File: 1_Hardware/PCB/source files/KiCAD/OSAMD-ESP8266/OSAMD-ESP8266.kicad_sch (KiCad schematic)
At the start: 20 parts, among them J1 DHT-Socket, J2 MQ-135 Conn, J3 LCD Conn, J6 USB_B, J7 Socket_D1_Mini_01_08, J8 Socket_D1_Mini_09_16, SW1 SW_Pushbutton, U1 WeMos_D1_mini

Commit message: switched button and buzzer pin
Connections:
- net BTN: now also J8.3 (Pin_3), U1.11 (D4); no longer J7.7 (Pin_7), U1.7 (CS/D8)
- net BUZZER: now also J7.7 (Pin_7), U1.7 (CS/D8); no longer J8.3 (Pin_3), U1.11 (D4)
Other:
- moved on the sheet: PullupBTN1, SW1

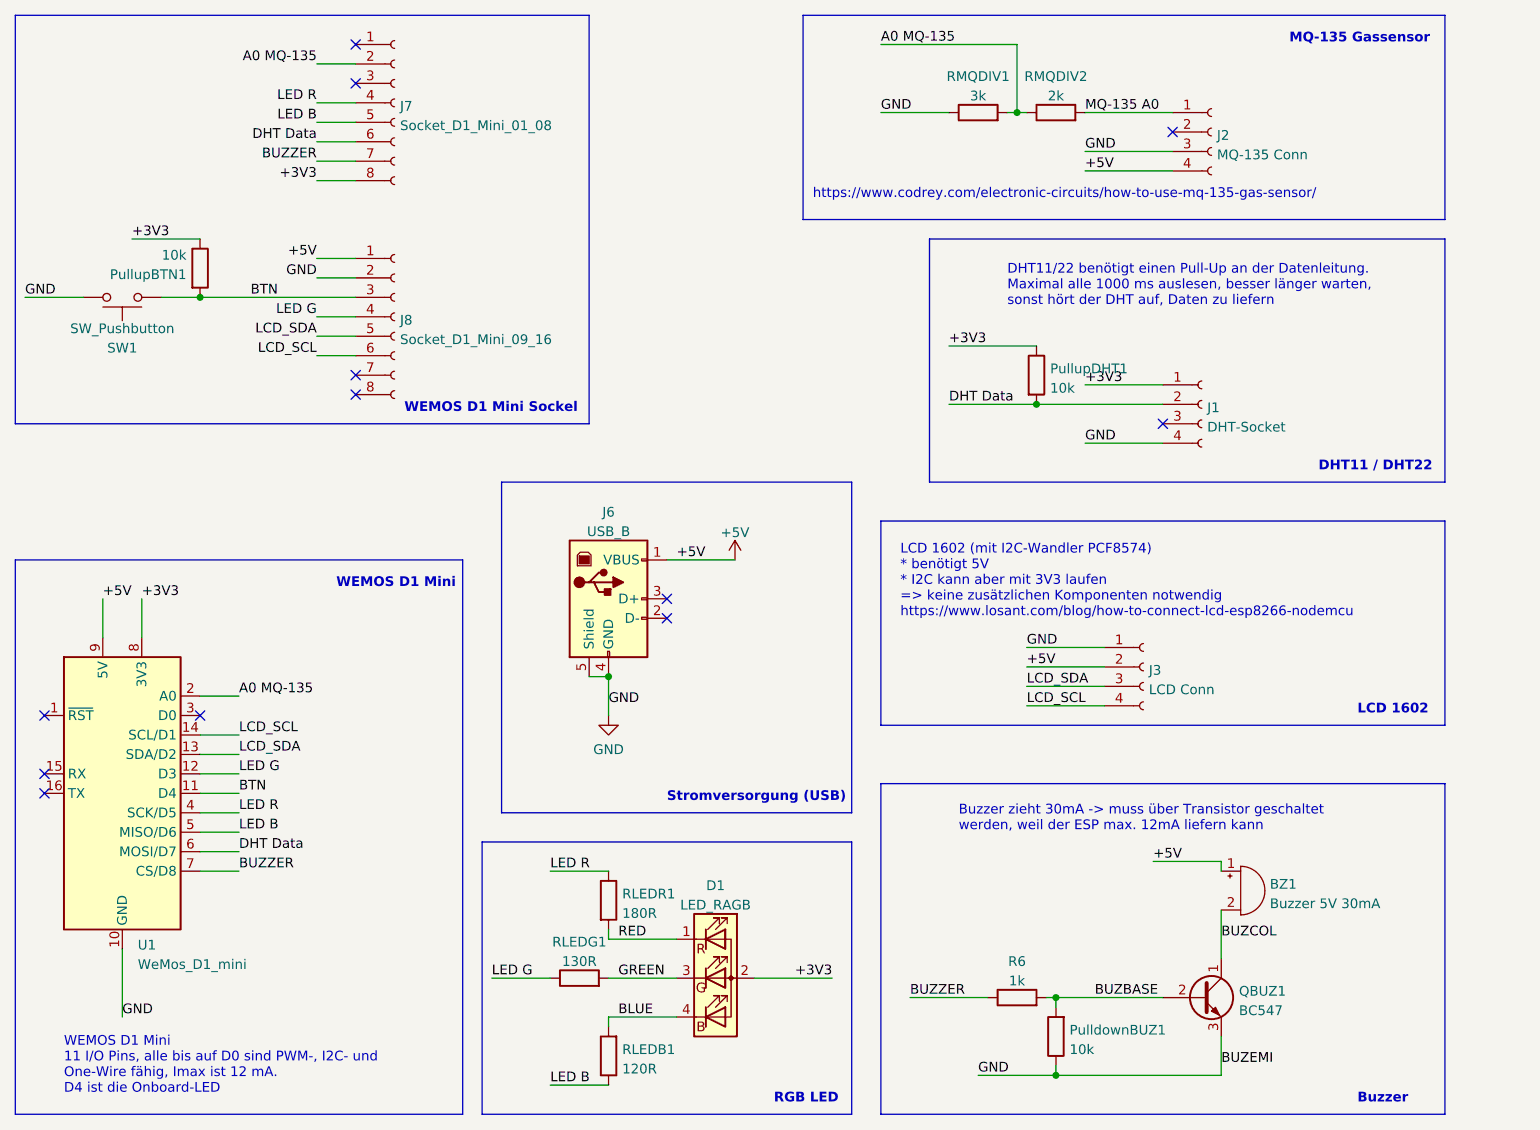
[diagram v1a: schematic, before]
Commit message: rounded edges on the pcb set gerber settings for jlcpcb
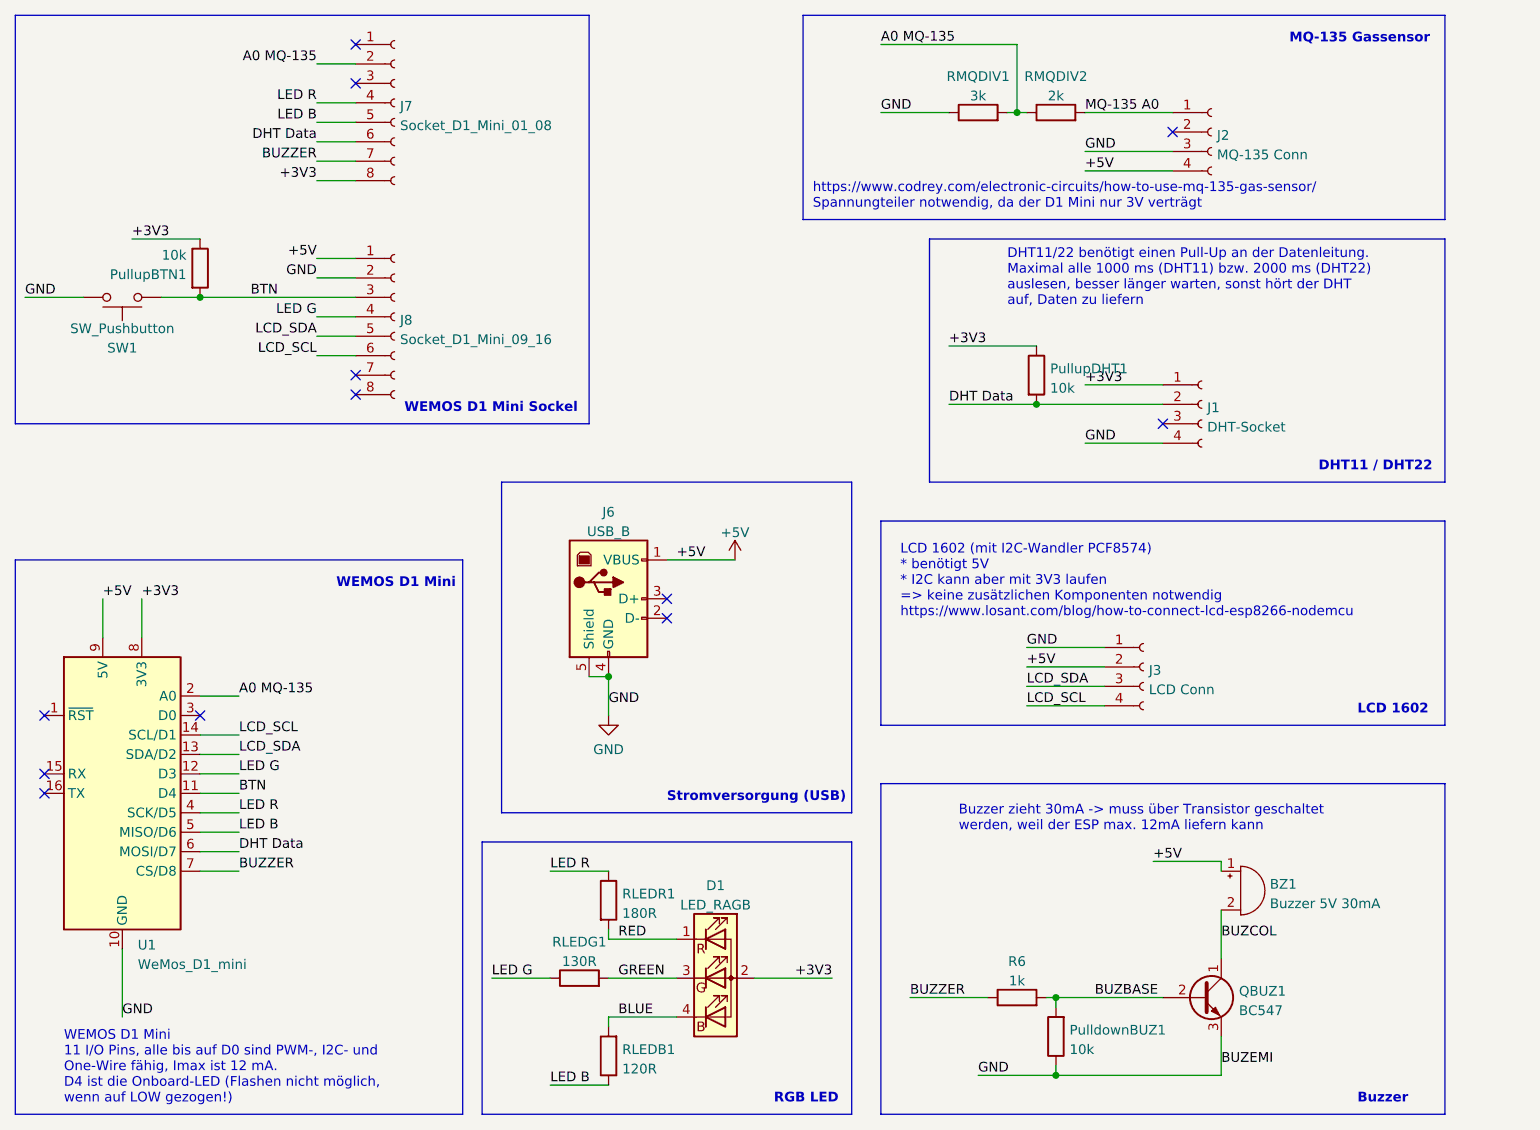
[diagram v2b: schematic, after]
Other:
- note added: "DHT11/22 benötigt einen Pull-Up an der Datenleitung. Maximal alle 1000 ms (DHT11) bzw. 2000 ms (DHT22) auslesen, besser länger warten, sonst hört der DHT auf, Daten zu liefern"
- note added: "WEMOS D1 Mini 11 I/O Pins, alle bis auf D0 sind PWM-, I2C- und One-Wire fähig, Imax ist 12 mA. D4 ist die Onboard-LED (Flashen nicht möglich, wenn auf LOW gezogen!)"
- note added: "https://www.codrey.com/electronic-circuits/how-to-use-mq-135-gas-sensor/ Spannungteiler notwendig, da der D1 Mini nur 3V verträgt"
- note removed: "DHT11/22 benötigt einen Pull-Up an der Datenleitung. Maximal alle 1000 ms auslesen, besser länger warten, sonst hört der DHT auf, Daten zu liefern"
- note removed: "WEMOS D1 Mini 11 I/O Pins, alle bis auf D0 sind PWM-, I2C- und One-Wire fähig, Imax ist 12 mA. D4 ist die Onboard-LED"
- note removed: "https://www.codrey.com/electronic-circuits/how-to-use-mq-135-gas-sensor/"
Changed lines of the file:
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@@
     (effects (font (size 1.27 1.27)) (justify left bottom))
   )
-  (text "https://www.codrey.com/electronic-circuits/how-to-use-mq-135-gas-sensor/"
-    (at 160.02 43.18 0)
+  (text "https://www.codrey.com/electronic-circuits/how-to-use-mq-135-gas-sensor/\nSpannungteiler notwendig, da der D1 Mini nur 3V verträgt"
+    (at 160.02 44.45 0)
     (effects (font (size 1.27 1.27)) (justify left bottom))
   )
@@
     (effects (font (size 1.27 1.27) (thickness 0.254) bold) (justify left bottom))
   )
-  (text "WEMOS D1 Mini\n11 I/O Pins, alle bis auf D0 sind PWM-, I2C- und \nOne-Wire fähig, Imax ist 12 mA.\nD4 ist die Onboard-LED"
-    (at 62.23 160.02 0)
+  (text "WEMOS D1 Mini\n11 I/O Pins, alle bis auf D0 sind PWM-, I2C- und \nOne-Wire fähig, Imax ist 12 mA.\nD4 ist die Onboard-LED (Flashen nicht möglich,\nwenn auf LOW gezogen!)"
+    (at 62.23 161.29 0)
     (effects (font (size 1.27 1.27)) (justify left bottom))
   )
-  (text "DHT11/22 benötigt einen Pull-Up an der Datenleitung.\nMaximal alle 1000 ms auslesen, besser länger warten,\nsonst hört der DHT auf, Daten zu liefern"
+  (text "DHT11/22 benötigt einen Pull-Up an der Datenleitung.\nMaximal alle 1000 ms (DHT11) bzw. 2000 ms (DHT22)\nauslesen, besser länger warten, sonst hört der DHT\nauf, Daten zu liefern"
     (at 185.42 57.15 0)
     (effects (font (size 1.27 1.27)) (justify left bottom))
